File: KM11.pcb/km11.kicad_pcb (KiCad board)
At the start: 2 copper layers, 62.4 x 214.1 mm, 56 parts, among them J1 PDP11 FlipChipSlot2x18, J10 ARDUINO POWER, J11 AUX, J2 PASS_OUT00, J3 PASS_OUT01, J4 POWER, J5 µTracer11 2x17 IDC, J6 PASS_OUT10, J7 PASS_OUT11, J8 GND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

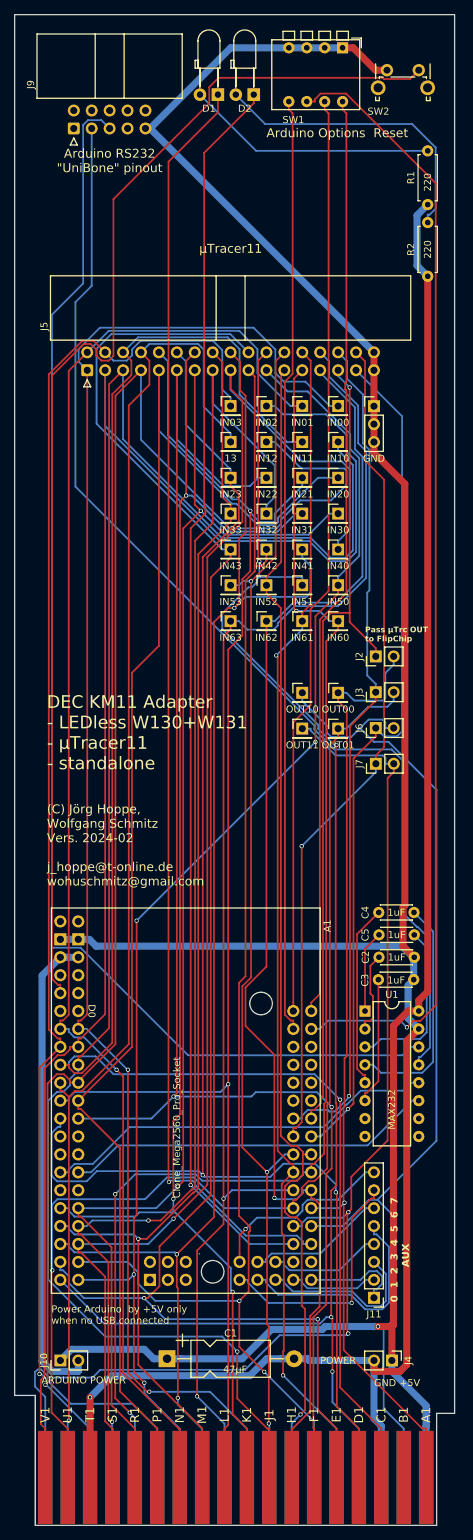
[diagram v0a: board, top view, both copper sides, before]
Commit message: Fix of KM11 wiring out01 <-> out10
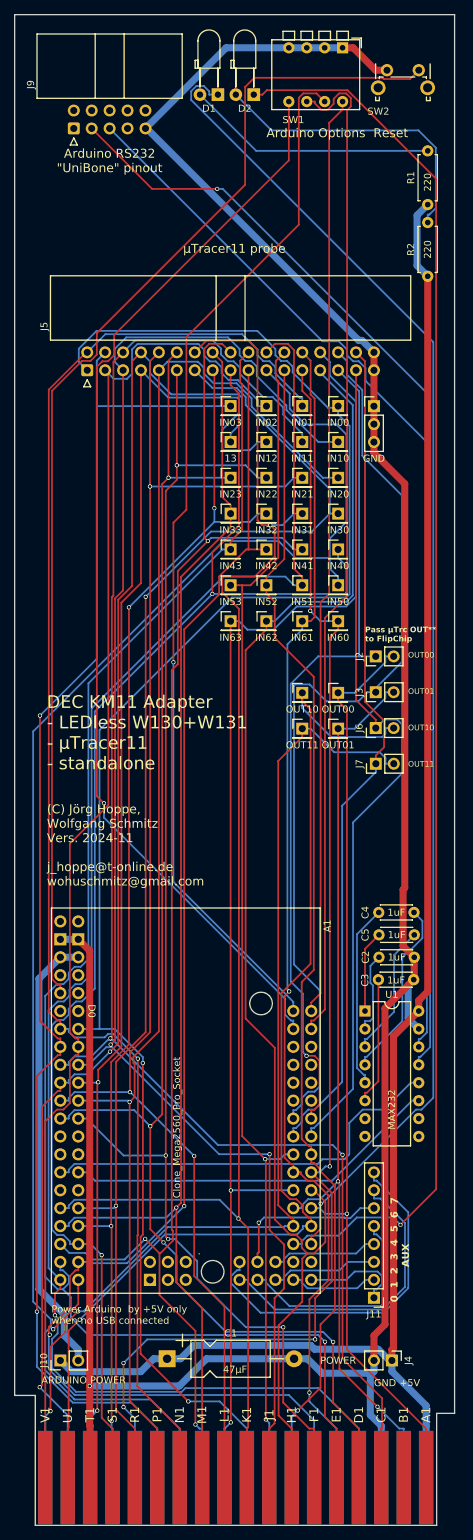
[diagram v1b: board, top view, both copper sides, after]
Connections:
- net TRACER_OUT10 renamed TRACER_OUT10_L
- A1 pad D40: PDP_OUT10 -> PDP_OUT10_L
- J1 pad B2: PDP_OUT10 -> PDP_OUT01_L
- J1 pad U1: PDP_OUT01_L -> PDP_OUT10_L
- J6 pad 2: PDP_OUT10 -> PDP_OUT10_L
- TP31 pad 1: PDP_OUT10 -> PDP_OUT10_L
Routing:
- net PDP_OUT10_L: track 0.00 -> 153.9 mm, vias 0 -> 1
- net PDP_OUT10: track 141.8 -> 0.00 mm
- net IN02: track 238.8 -> 189.5 mm
- net IN12: track 225.4 -> 187.4 mm, vias 1 -> 2
- net IN50: track 182.3 -> 217.9 mm, vias 4 -> 1
- net Net-(J9-TXD): track 181.7 -> 151.2 mm
- net PDP_OUT01_L: track 153.5 -> 123.2 mm, vias 1 -> 2
- net IN10: track 245.4 -> 216.5 mm, vias 1 -> 2
- net /arduino/AUX7: track 27.0 -> 50.7 mm, vias 1 -> 0
- net /arduino/LED2: track 176.4 -> 199.1 mm
- net IN22: track 215.0 -> 192.5 mm, vias 2 -> 4
- net IN32: track 192.1 -> 169.9 mm, vias 2 -> 4
- net Net-(A1-PadA3): track 132.8 -> 154.9 mm, vias 0 -> 1
- net PDP_OUT11_L: track 165.3 -> 143.7 mm
- net IN43: track 230.7 -> 209.1 mm, vias 2 -> 1
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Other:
- board text added: "(C) Jörg Hoppe, Wolfgang Schmitz Vers. 2024-11 j_hoppe@t-online.de wohuschmitz@gmail.com"
- board text added: "OUT00 OUT01 OUT10 OUT11"
- board text added: "Pass µTrc OUT** to FlipChip"
- board text added: "µTracer11 probe"
- board text removed: "(C) Jörg Hoppe, Wolfgang Schmitz Vers. 2024-02 j_hoppe@t-online.de wohuschmitz@gmail.com"
- board text removed: "Pass µTrc OUT to FlipChip"
- board text removed: "µTracer11"

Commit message: ^repalce synthetic KM11 signals "Inxx, out**" with flipchip pin names
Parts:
- J2: value PASS_OUT00 -> PASS_A1
- J3: value PASS_OUT01 -> PASS_B2
- J6: value PASS_OUT10 -> PASS_U1
- J7: value PASS_OUT11 -> PASS_V2
- TP1: value IN60 -> R2
- TP10: value IN41 -> M2
- TP11: value IN31 -> K1
- TP12: value IN21 -> L1
- TP13: value IN11 -> C1
- TP14: value IN01 -> N1
- TP15: value IN62 -> H1
- TP16: value IN52 -> H2
- TP17: value IN42 -> F2
- TP18: value IN32 -> S2
- TP19: value IN22 -> F1
- TP2: value IN50 -> N2
- TP20: value IN12 -> T2
- TP21: value IN02 -> V1
- TP22: value IN63 -> L2
- TP23: value IN53 -> J2
- TP24: value IN43 -> E1
- TP25: value IN33 -> M1
- TP26: value IN23 -> D1
- TP27: value 13 -> U2
- TP28: value IN03 -> P2
- TP29: value OUT00 -> A1
- TP3: value IN40 -> S1
- TP30: value OUT01 -> B2
- TP31: value OUT10 -> U1
- TP32: value OUT11 -> V2
- TP4: value IN30 -> R1
- TP5: value IN20 -> P1
- TP6: value IN10 -> J1
- TP7: value IN00 -> K2
- TP8: value IN61 -> E2
- TP9: value IN51 -> D2
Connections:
- net IN00 renamed K2
- net IN01 renamed N1
- net IN02 renamed V1
- net IN03 renamed P2
- net IN10 renamed J1
- net IN11 renamed C1
- net IN12 renamed T2
- net IN13 renamed U2
- net IN20 renamed P1
- net IN21 renamed L1
- net IN22 renamed F1
- net IN23 renamed D1
- net IN30 renamed R1
- net IN31 renamed K1
- net IN32 renamed S2
- net IN33 renamed M1
- net IN40 renamed S1
- net IN41 renamed M2
- net IN42 renamed F2
- net IN43 renamed E1
- net IN50 renamed N2
- net IN51 renamed D2
- net IN52 renamed H2
- net IN53 renamed J2
- net IN60 renamed R2
- net IN61 renamed E2
- net IN62 renamed H1
- net IN63 renamed L2
- net PDP_OUT00_L renamed PDP_A1_L
- net PDP_OUT01_L renamed PDP_B2_L
- net PDP_OUT10_L renamed PDP_U1_L
- net PDP_OUT11_L renamed PDP_V2_L
- net TRACER_OUT00_L renamed TRACER_A1_L
- net TRACER_OUT01_L renamed TRACER_B2_L
- net TRACER_OUT10_L renamed TRACER_U1_L
- net TRACER_OUT11_L renamed TRACER_V2_L
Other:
- board text added: "A1 B2 U1 V2"
- board text removed: "OUT00 OUT01 OUT10 OUT11"
